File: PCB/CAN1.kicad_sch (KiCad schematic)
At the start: 7 parts, among them U2 ISO1044BD

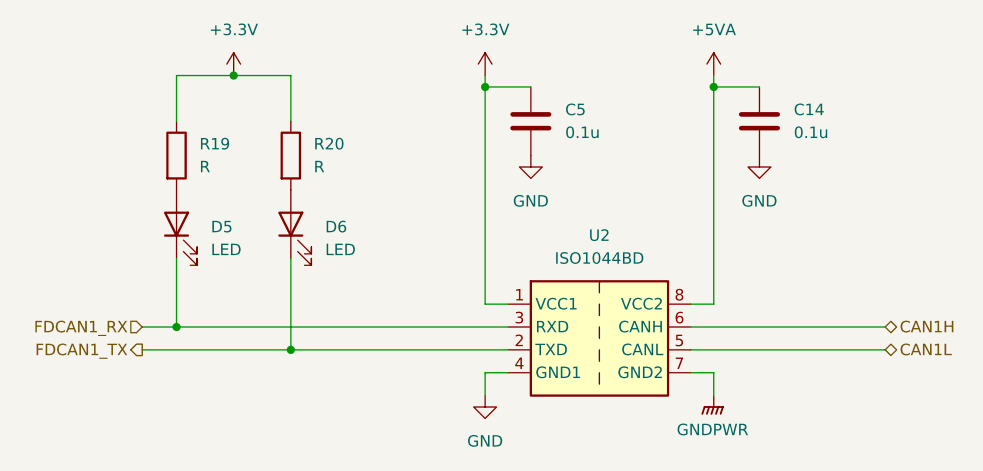
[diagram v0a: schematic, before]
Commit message: 電源以外配線おわり
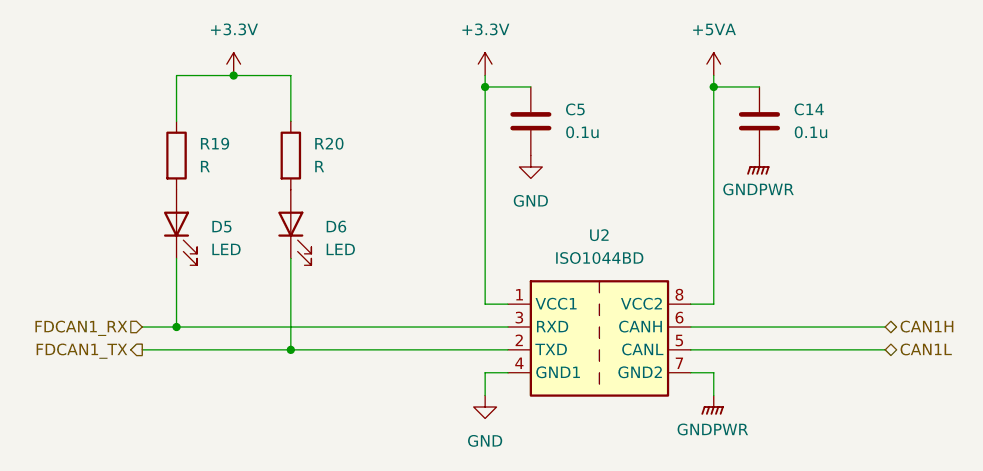
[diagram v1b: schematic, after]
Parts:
- C14, C5: footprint Capacitor_SMD:C_0402_1005Metric_Pad0.74x0.62mm_HandSolder -> Capacitor_SMD:C_0603_1608Metric_Pad1.08x0.95mm_HandSolder
- R19, R20: footprint Resistor_SMD:R_0402_1005Metric_Pad0.72x0.64mm_HandSolder -> Resistor_SMD:R_0603_1608Metric_Pad0.98x0.95mm_HandSolder
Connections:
- net GND: no longer C14.2
- net GNDPWR: now also C14.2
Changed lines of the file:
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@@
+	)
+	(symbol
+		(lib_id "power:GNDPWR")
+		(at 173.99 76.2 0)
+		(unit 1)
+		(exclude_from_sim no)
+		(in_bom yes)
+		(on_board yes)
+		(dnp no)
+		(fields_autoplaced yes)
+		(property "Reference" "#PWR067"
+			(at 173.99 81.28 0)
+			(effects
+				(font
+					(size 1.27 1.27)
+				)
+				(hide yes)
+			)
+		)
+		(property "Value" "GNDPWR"
+			(at 173.863 80.01 0)
+			(effects
+				(font
+					(size 1.27 1.27)
+				)
+			)
+		)
+		(property "Footprint" ""
+			(at 173.99 77.47 0)
+			(effects
+				(font
+					(size 1.27 1.27)
+				)
+				(hide yes)
+			)
+		)
+		(property "Datasheet" ""
+			(at 173.99 77.47 0)
+			(effects
+				(font
+					(size 1.27 1.27)
+				)
+				(hide yes)
+			)
+		)
+		(property "Description" "Power symbol creates a global label with name \"GNDPWR\" , global ground"
+			(at 173.99 76.2 0)
+			(effects
+				(font
+					(size 1.27 1.27)
+				)
+				(hide yes)
+			)
+		)
+		(pin "1"
+		)
+		(instances
+			(project "kaniharu"
+				(path "/8cdd0db5-06ad-47be-921f-3bd5b446781a/b6046ddf-7fdc-41dc-9f1d-fd97953c30cb"
+					(reference "#PWR067")
+					(unit 1)
+				)
+			)
+		)
 	)
 	(symbol
@@
 			)
 		)
-		(property "Footprint" "Capacitor_SMD:C_0402_1005Metric_Pad0.74x0.62mm_HandSolder"
+		(property "Footprint" "Capacitor_SMD:C_0603_1608Metric_Pad1.08x0.95mm_HandSolder"
 			(at 174.9552 76.2 0)
 			(effects
@@
 			)
 		)
-		(property "Footprint" "Resistor_SMD:R_0402_1005Metric_Pad0.72x0.64mm_HandSolder"
+		(property "Footprint" "Resistor_SMD:R_0603_1608Metric_Pad0.98x0.95mm_HandSolder"
 			(at 120.142 76.2 90)
 			(effects
@@
 	)
 	(symbol
-		(lib_id "power:GND")
-		(at 173.99 76.2 0)
-		(unit 1)
-		(exclude_from_sim no)
-		(in_bom yes)
-		(on_board yes)
-		(dnp no)
-		(fields_autoplaced yes)
-		(property "Reference" "#PWR020"
-			(at 173.99 82.55 0)
-			(effects
-				(font
-					(size 1.27 1.27)
-				)
-				(hide yes)
-			)
-		)
-		(property "Value" "GND"
-			(at 173.99 81.28 0)
-			(effects
-				(font
-					(size 1.27 1.27)
-				)
-			)
-		)
-		(property "Footprint" ""
-			(at 173.99 76.2 0)
-			(effects
-				(font
-					(size 1.27 1.27)
-				)
-				(hide yes)
-			)
-		)
-		(property "Datasheet" ""
-			(at 173.99 76.2 0)
-			(effects
-				(font
-					(size 1.27 1.27)
-				)
-				(hide yes)
-			)
-		)
-		(property "Description" "Power symbol creates a global label with name \"GND\" , ground"
-			(at 173.99 76.2 0)
-			(effects
-				(font
-					(size 1.27 1.27)
-				)
-				(hide yes)
-			)
-		)
-		(pin "1"
-		)
-		(instances
-			(project "kaniharu"
-				(path "/8cdd0db5-06ad-47be-921f-3bd5b446781a/b6046ddf-7fdc-41dc-9f1d-fd97953c30cb"
-					(reference "#PWR020")
-					(unit 1)
-				)
-			)
-		)
-	)
-	(symbol
 		(lib_id "power:+5VA")
 		(at 168.91 67.31 0)
@@
 			)
 		)
-		(property "Footprint" "Resistor_SMD:R_0402_1005Metric_Pad0.72x0.64mm_HandSolder"
+		(property "Footprint" "Resistor_SMD:R_0603_1608Metric_Pad0.98x0.95mm_HandSolder"
 			(at 107.442 76.2 90)
 			(effects
@@
 			)
 		)
-		(property "Footprint" "Capacitor_SMD:C_0402_1005Metric_Pad0.74x0.62mm_HandSolder"
+		(property "Footprint" "Capacitor_SMD:C_0603_1608Metric_Pad1.08x0.95mm_HandSolder"
 			(at 149.5552 76.2 0)
 			(effects

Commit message: update:基板発注した
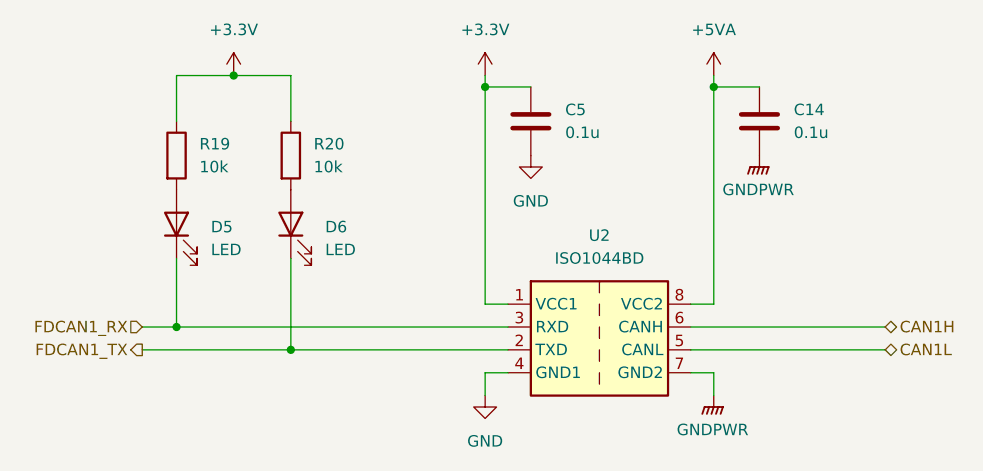
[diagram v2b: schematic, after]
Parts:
- R19, R20: value R -> 10k
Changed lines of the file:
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@@
 			)
 		)
-		(property "Value" "R"
+		(property "Value" "10k"
 			(at 124.46 77.4699 0)
 			(effects
@@
 			)
 		)
-		(property "Value" "R"
+		(property "Value" "10k"
 			(at 111.76 77.4699 0)
 			(effects
